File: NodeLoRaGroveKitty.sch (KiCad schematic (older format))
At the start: 39 parts, among them P1 PICKIT PROGRAMMER, P2 Battery, P3 A0, P4 D9, P5 USB-Serial, P6 I2C, SW1 SW_BOOT, SW2 SW_RESET, U1 AP2114, U2 MCP73831T-2ATI/OT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

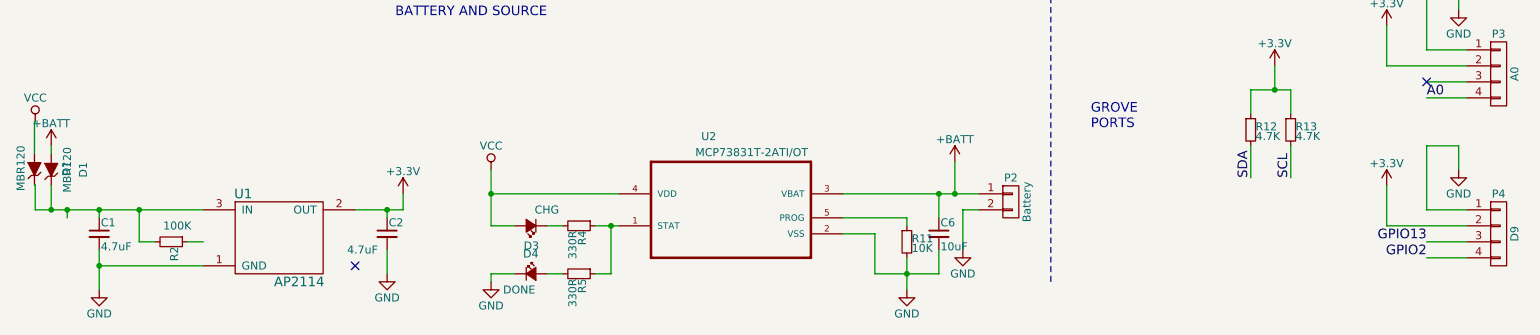
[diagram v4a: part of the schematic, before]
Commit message: Change D2 for D13
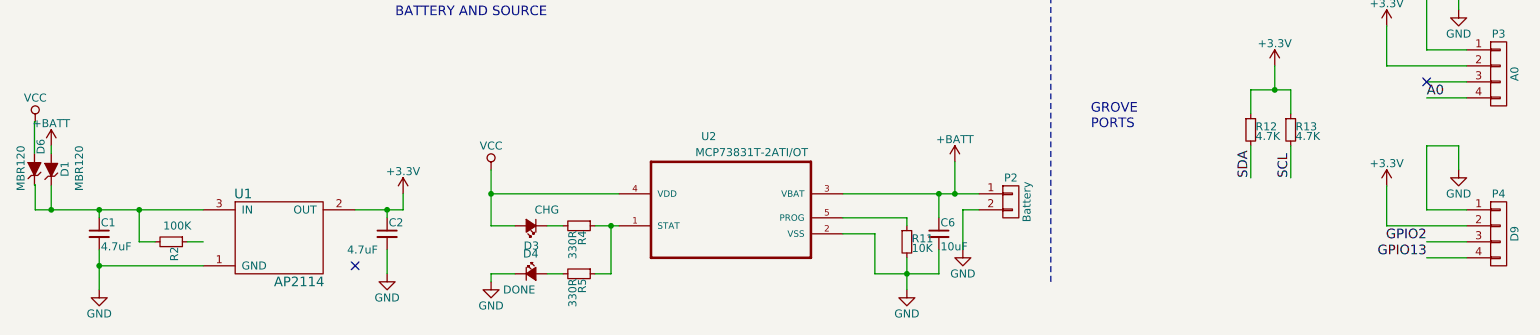
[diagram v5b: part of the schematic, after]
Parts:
- gave numbers to parts that had none: 1
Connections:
- net GPIO13: now also P4.4 (P4); no longer P4.3 (P3)
- net GPIO2: now also P4.3 (P3); no longer P4.4 (P4)
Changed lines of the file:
@@
 NoConn ~ 1450 2250
 $Comp
-L +3.3V #PWR01
+L +3.3V #PWR9
 U 1 1 57D06DBD
 P 3200 800
-F 0 "#PWR01" H 3200 650 50  0001 C CNN
+F 0 "#PWR9" H 3200 650 50  0001 C CNN
 F 1 "+3.3V" H 3200 940 50  0000 C CNN
 F 2 "" H 3200 800 50  0000 C CNN
@@
 $EndComp
 $Comp
-L GND #PWR02
+L GND #PWR10
 U 1 1 57D06E12
 P 3250 3400
-F 0 "#PWR02" H 3250 3150 50  0001 C CNN
+F 0 "#PWR10" H 3250 3150 50  0001 C CNN
 F 1 "GND" H 3250 3250 50  0000 C CNN
 F 2 "" H 3250 3400 50  0000 C CNN
@@
 $EndComp
 $Comp
-L GND #PWR03
+L GND #PWR4
 U 1 1 57D1B92A
 P 1000 6600
-F 0 "#PWR03" H 1000 6350 50  0001 C CNN
+F 0 "#PWR4" H 1000 6350 50  0001 C CNN
 F 1 "GND" H 1000 6450 50  0000 C CNN
 F 2 "" H 1000 6600 50  0000 C CNN
@@
 U 1 1 57D1B9F5
 P 700 5850
-F 0 "D1" H 700 5650 50  0000 C CNN
-F 1 "MBR120" H 700 5750 50  0000 C CNN
+F 0 "D1" H 705 5765 50  0000 C CNN
+F 1 "MBR120" H 710 5675 50  0000 C CNN
 F 2 "Diodes_SMD:SOD-123" H 700 5850 50  0001 C CNN
 F 3 "" H 700 5850 50  0000 C CNN
@@
 NoConn ~ 2600 6450
 $Comp
-L +3.3V #PWR04
+L +3.3V #PWR7
 U 1 1 57D1BDB1
 P 2900 6000
-F 0 "#PWR04" H 2900 5850 50  0001 C CNN
+F 0 "#PWR7" H 2900 5850 50  0001 C CNN
 F 1 "+3.3V" H 2900 6140 50  0000 C CNN
 F 2 "" H 2900 6000 50  0000 C CNN
@@
 $EndComp
 $Comp
-L VCC #PWR05
+L VCC #PWR2
 U 1 1 57D1BE36
 P 600 5550
-F 0 "#PWR05" H 600 5400 50  0001 C CNN
+F 0 "#PWR2" H 600 5400 50  0001 C CNN
 F 1 "VCC" H 600 5700 50  0000 C CNN
 F 2 "" H 600 5550 50  0000 C CNN
@@
 $EndComp
 $Comp
-L +BATT #PWR06
+L +BATT #PWR3
 U 1 1 57D1BE7A
 P 700 5700
-F 0 "#PWR06" H 700 5550 50  0001 C CNN
+F 0 "#PWR3" H 700 5550 50  0001 C CNN
 F 1 "+BATT" H 700 5840 50  0000 C CNN
 F 2 "" H 700 5700 50  0000 C CNN
@@
 $EndComp
 $Comp
-L GND #PWR07
+L GND #PWR23
 U 1 1 57D1D194
 P 6050 6600
-F 0 "#PWR07" H 6050 6350 50  0001 C CNN
+F 0 "#PWR23" H 6050 6350 50  0001 C CNN
 F 1 "GND" H 6050 6450 50  0000 C CNN
 F 2 "" H 6050 6600 50  0000 C CNN
@@
 $EndComp
 $Comp
-L VCC #PWR08
+L VCC #PWR12
 U 1 1 57D1D1DE
 P 3450 5850
-F 0 "#PWR08" H 3450 5700 50  0001 C CNN
+F 0 "#PWR12" H 3450 5700 50  0001 C CNN
 F 1 "VCC" H 3450 6000 50  0000 C CNN
 F 2 "" H 3450 5850 50  0000 C CNN
@@
 $EndComp
 $Comp
-L +BATT #PWR09
+L +BATT #PWR24
 U 1 1 57D1DA2B
 P 6350 5800
-F 0 "#PWR09" H 6350 5650 50  0001 C CNN
+F 0 "#PWR24" H 6350 5650 50  0001 C CNN
 F 1 "+BATT" H 6350 5940 50  0000 C CNN
 F 2 "" H 6350 5800 50  0000 C CNN
@@
 $EndComp
 $Comp
-L GND #PWR010
+L GND #PWR25
 U 1 1 57D1DBC4
 P 6400 6350
-F 0 "#PWR010" H 6400 6100 50  0001 C CNN
+F 0 "#PWR25" H 6400 6100 50  0001 C CNN
 F 1 "GND" H 6400 6200 50  0000 C CNN
 F 2 "" H 6400 6350 50  0000 C CNN
@@
 $EndComp
 $Comp
-L GND #PWR011
+L GND #PWR13
 U 1 1 57D1E0B8
 P 3450 6550
-F 0 "#PWR011" H 3450 6300 50  0001 C CNN
+F 0 "#PWR13" H 3450 6300 50  0001 C CNN
 F 1 "GND" H 3450 6400 50  0000 C CNN
 F 2 "" H 3450 6550 50  0000 C CNN
@@
 $EndComp
 $Comp
-L +3.3V #PWR012
+L +3.3V #PWR28
 U 1 1 57D1F885
 P 8350 5200
-F 0 "#PWR012" H 8350 5050 50  0001 C CNN
+F 0 "#PWR28" H 8350 5050 50  0001 C CNN
 F 1 "+3.3V" H 8350 5340 50  0000 C CNN
 F 2 "" H 8350 5200 50  0000 C CNN
@@
 $EndComp
 $Comp
-L GND #PWR013
+L GND #PWR17
 U 1 1 57D20110
 P 4400 1550
-F 0 "#PWR013" H 4400 1300 50  0001 C CNN
+F 0 "#PWR17" H 4400 1300 50  0001 C CNN
 F 1 "GND" H 4400 1400 50  0000 C CNN
 F 2 "" H 4400 1550 50  0000 C CNN
@@
 $EndComp
 $Comp
-L +3.3V #PWR014
+L +3.3V #PWR22
 U 1 1 57D20695
 P 5300 900
-F 0 "#PWR014" H 5300 750 50  0001 C CNN
+F 0 "#PWR22" H 5300 750 50  0001 C CNN
 F 1 "+3.3V" H 5300 1040 50  0000 C CNN
 F 2 "" H 5300 900 50  0000 C CNN
@@
 SDA
 $Comp
-L GND #PWR015
+L GND #PWR36
 U 1 1 57D20B0E
 P 10700 4850
-F 0 "#PWR015" H 10700 4600 50  0001 C CNN
+F 0 "#PWR36" H 10700 4600 50  0001 C CNN
 F 1 "GND" H 10700 4700 50  0000 C CNN
 F 2 "" H 10700 4850 50  0000 C CNN
@@
 $EndComp
 $Comp
-L +3.3V #PWR016
+L +3.3V #PWR14
 U 1 1 57D218AC
 P 3650 2350
-F 0 "#PWR016" H 3650 2200 50  0001 C CNN
+F 0 "#PWR14" H 3650 2200 50  0001 C CNN
 F 1 "+3.3V" H 3650 2490 50  0000 C CNN
 F 2 "" H 3650 2350 50  0000 C CNN
@@
 A0
 $Comp
-L GND #PWR017
+L GND #PWR31
 U 1 1 57D2307B
 P 9500 4850
-F 0 "#PWR017" H 9500 4600 50  0001 C CNN
+F 0 "#PWR31" H 9500 4600 50  0001 C CNN
 F 1 "GND" H 9500 4700 50  0000 C CNN
 F 2 "" H 9500 4850 50  0000 C CNN
@@
 $EndComp
 Text Label 9300 6400 2    60   ~ 0
+GPIO13
+Text Label 9300 6300 2    60   ~ 0
 GPIO2
-Text Label 9300 6300 2    60   ~ 0
-GPIO13
-$Comp
-L GND #PWR018
+$Comp
+L GND #PWR32
 U 1 1 57D230E6
 P 9500 5850
-F 0 "#PWR018" H 9500 5600 50  0001 C CNN
+F 0 "#PWR32" H 9500 5600 50  0001 C CNN
 F 1 "GND" H 9500 5700 50  0000 C CNN
 F 2 "" H 9500 5850 50  0000 C CNN
@@
 $EndComp
 $Comp
-L GND #PWR019
+L GND #PWR11
 U 1 1 57D23805
 P 3450 1250
-F 0 "#PWR019" H 3450 1000 50  0001 C CNN
+F 0 "#PWR11" H 3450 1000 50  0001 C CNN
 F 1 "GND" H 3450 1100 50  0000 C CNN
 F 2 "" H 3450 1250 50  0000 C CNN
@@
 $EndComp
 $Comp
-L GND #PWR021
+L GND #PWR15
 U 1 1 57D25846
 P 3850 1250
-F 0 "#PWR021" H 3850 1000 50  0001 C CNN
+F 0 "#PWR15" H 3850 1000 50  0001 C CNN
 F 1 "GND" H 3850 1100 50  0000 C CNN
 F 2 "" H 3850 1250 50  0000 C CNN
@@
 $EndComp
 $Comp
-L GND #PWR022
+L GND #PWR5
 U 1 1 57D2E394
 P 1500 850
-F 0 "#PWR022" H 1500 600 50  0001 C CNN
+F 0 "#PWR5" H 1500 600 50  0001 C CNN
 F 1 "GND" H 1500 700 50  0000 C CNN
 F 2 "" H 1500 850 50  0000 C CNN
@@
 $EndComp
 $Comp
-L GND #PWR023
+L GND #PWR1
 U 1 1 57D2E541
 P 600 950
-F 0 "#PWR023" H 600 700 50  0001 C CNN
+F 0 "#PWR1" H 600 700 50  0001 C CNN
 F 1 "GND" H 600 800 50  0000 C CNN
 F 2 "" H 600 950 50  0000 C CNN
@@
 $EndComp
 $Comp
-L GND #PWR024
+L GND #PWR6
 U 1 1 57D3198A
 P 2800 6500
-F 0 "#PWR024" H 2800 6250 50  0001 C CNN
+F 0 "#PWR6" H 2800 6250 50  0001 C CNN
 F 1 "GND" H 2800 6350 50  0000 C CNN
 F 2 "" H 2800 6500 50  0000 C CNN
@@
 $EndComp
 $Comp
-L GND #PWR025
+L GND #PWR8
 U 1 1 57D378F3
 P 3150 3000
-F 0 "#PWR025" H 3150 2750 50  0001 C CNN
+F 0 "#PWR8" H 3150 2750 50  0001 C CNN
 F 1 "GND" H 3150 2850 50  0000 C CNN
 F 2 "" H 3150 3000 50  0000 C CNN
@@
 RST
 $Comp
-L GND #PWR026
+L GND #PWR34
 U 1 1 5807D443
 P 9925 1885
-F 0 "#PWR026" H 9925 1635 50  0001 C CNN
+F 0 "#PWR34" H 9925 1635 50  0001 C CNN
 F 1 "GND" H 9925 1735 50  0000 C CNN
 F 2 "" H 9925 1885 50  0000 C CNN
@@
 $EndComp
 $Comp
-L +3.3V #PWR027
+L +3.3V #PWR27
 U 1 1 5807DA5B
 P 7425 1885
-F 0 "#PWR027" H 7425 1735 50  0001 C CNN
+F 0 "#PWR27" H 7425 1735 50  0001 C CNN
 F 1 "+3.3V" H 7425 2025 50  0000 C CNN
 F 2 "" H 7425 1885 50  0000 C CNN
@@
 $EndComp
 $Comp
-L GND #PWR028
+L GND #PWR20
 U 1 1 58092ECC
 P 4840 3295
-F 0 "#PWR028" H 4840 3045 50  0001 C CNN
+F 0 "#PWR20" H 4840 3045 50  0001 C CNN
 F 1 "GND" H 4840 3145 50  0000 C CNN
 F 2 "" H 4840 3295 50  0000 C CNN
@@
 $EndComp
 $Comp
-L +3.3V #PWR029
+L +3.3V #PWR18
 U 1 1 58094181
 P 4540 2635
-F 0 "#PWR029" H 4540 2485 50  0001 C CNN
+F 0 "#PWR18" H 4540 2485 50  0001 C CNN
 F 1 "+3.3V" H 4540 2775 50  0000 C CNN
 F 2 "" H 4540 2635 50  0000 C CNN
@@
 $EndComp
 $Comp
-L GND #PWR030
+L GND #PWR19
 U 1 1 58098088
 P 4560 3870
-F 0 "#PWR030" H 4560 3620 50  0001 C CNN
+F 0 "#PWR19" H 4560 3620 50  0001 C CNN
 F 1 "GND" H 4560 3720 50  0000 C CNN
 F 2 "" H 4560 3870 50  0000 C CNN
@@
 TX
 $Comp
-L GND #PWR031
+L GND #PWR33
 U 1 1 5809B44C
 P 9805 3850
-F 0 "#PWR031" H 9805 3600 50  0001 C CNN
+F 0 "#PWR33" H 9805 3600 50  0001 C CNN
 F 1 "GND" H 9805 3700 50  0000 C CNN
 F 2 "" H 9805 3850 50  0000 C CNN
@@
 $EndComp
 $Comp
-L VCC #PWR032
+L VCC #PWR37
 U 1 1 5809B516
 P 10840 3935
-F 0 "#PWR032" H 10840 3785 50  0001 C CNN
+F 0 "#PWR37" H 10840 3785 50  0001 C CNN
 F 1 "VCC" H 10840 4085 50  0000 C CNN
 F 2 "" H 10840 3935 50  0000 C CNN
@@
 $EndComp
 $Comp
-L PWR_FLAG #FLG033
+L PWR_FLAG #FLG1
 U 1 1 5809BB20
 P 10550 3955
-F 0 "#FLG033" H 10550 4050 50  0001 C CNN
+F 0 "#FLG1" H 10550 4050 50  0001 C CNN
 F 1 "PWR_FLAG" H 10550 4135 50  0000 C CNN
 F 2 "" H 10550 3955 50  0000 C CNN
@@
 $EndComp
 $Comp
-L GND #PWR034
+L GND #PWR16
 U 1 1 5809F5BD
 P 4380 2115
-F 0 "#PWR034" H 4380 1865 50  0001 C CNN
+F 0 "#PWR16" H 4380 1865 50  0001 C CNN
 F 1 "GND" H 4380 1965 50  0000 C CNN
 F 2 "" H 4380 2115 50  0000 C CNN
@@
 $EndComp
 $Comp
-L +3.3V #PWR035
+L +3.3V #PWR29
 U 1 1 58514B84
 P 9050 4950
-F 0 "#PWR035" H 9050 4800 50  0001 C CNN
+F 0 "#PWR29" H 9050 4800 50  0001 C CNN
 F 1 "+3.3V" H 9050 5090 50  0000 C CNN
 F 2 "" H 9050 4950 50  0000 C CNN
@@
 $EndComp
 $Comp
-L +3.3V #PWR036
+L +3.3V #PWR35
 U 1 1 58514F58
 P 10250 4950
-F 0 "#PWR036" H 10250 4800 50  0001 C CNN
+F 0 "#PWR35" H 10250 4800 50  0001 C CNN
 F 1 "+3.3V" H 10250 5090 50  0000 C CNN
 F 2 "" H 10250 4950 50  0000 C CNN
@@
 $EndComp
 $Comp
-L +3.3V #PWR037
+L +3.3V #PWR30
 U 1 1 585150D6
 P 9050 5950
-F 0 "#PWR037" H 9050 5800 50  0001 C CNN
+F 0 "#PWR30" H 9050 5800 50  0001 C CNN
 F 1 "+3.3V" H 9050 6090 50  0000 C CNN
 F 2 "" H 9050 5950 50  0000 C CNN
@@
 GPIO2
 $Comp
-L +3.3V #PWR038
+L +3.3V #PWR21
 U 1 1 5854483F
 P 5160 2620
-F 0 "#PWR038" H 5160 2470 50  0001 C CNN
+F 0 "#PWR21" H 5160 2470 50  0001 C CNN
 F 1 "+3.3V" H 5160 2760 50  0000 C CNN
 F 2 "" H 5160 2620 50  0000 C CNN
@@
 $EndComp
 $Comp
-L ZENERsmall D?
+L ZENERsmall D6
 U 1 1 58924335
 P 595 5845
-F 0 "D?" H 595 5645 50  0000 C CNN
+F 0 "D6" H 735 5805 50  0000 C CNN
 F 1 "MBR120" H 600 5930 50  0000 C CNN
 F 2 "Diodes_SMD:SOD-123" H 595 5845 50  0001 C CNN
@@
 Wire Wire Line
 	1000 6100 1000 6150
-Connection ~ 800  6100
-Wire Wire Line
-	800  6100 800  6150
 Connection ~ 1250 6100
 Wire Wire Line
@@
 NoConn ~ 1450 2050
 $Comp
-L +3.3V #PWR?
+L +3.3V #PWR26
 U 1 1 58926B64
 P 6840 3940
-F 0 "#PWR?" H 6840 3790 50  0001 C CNN
+F 0 "#PWR26" H 6840 3790 50  0001 C CNN
 F 1 "+3.3V" H 6840 4080 50  0000 C CNN
 F 2 "" H 6840 3940 50  0000 C CNN

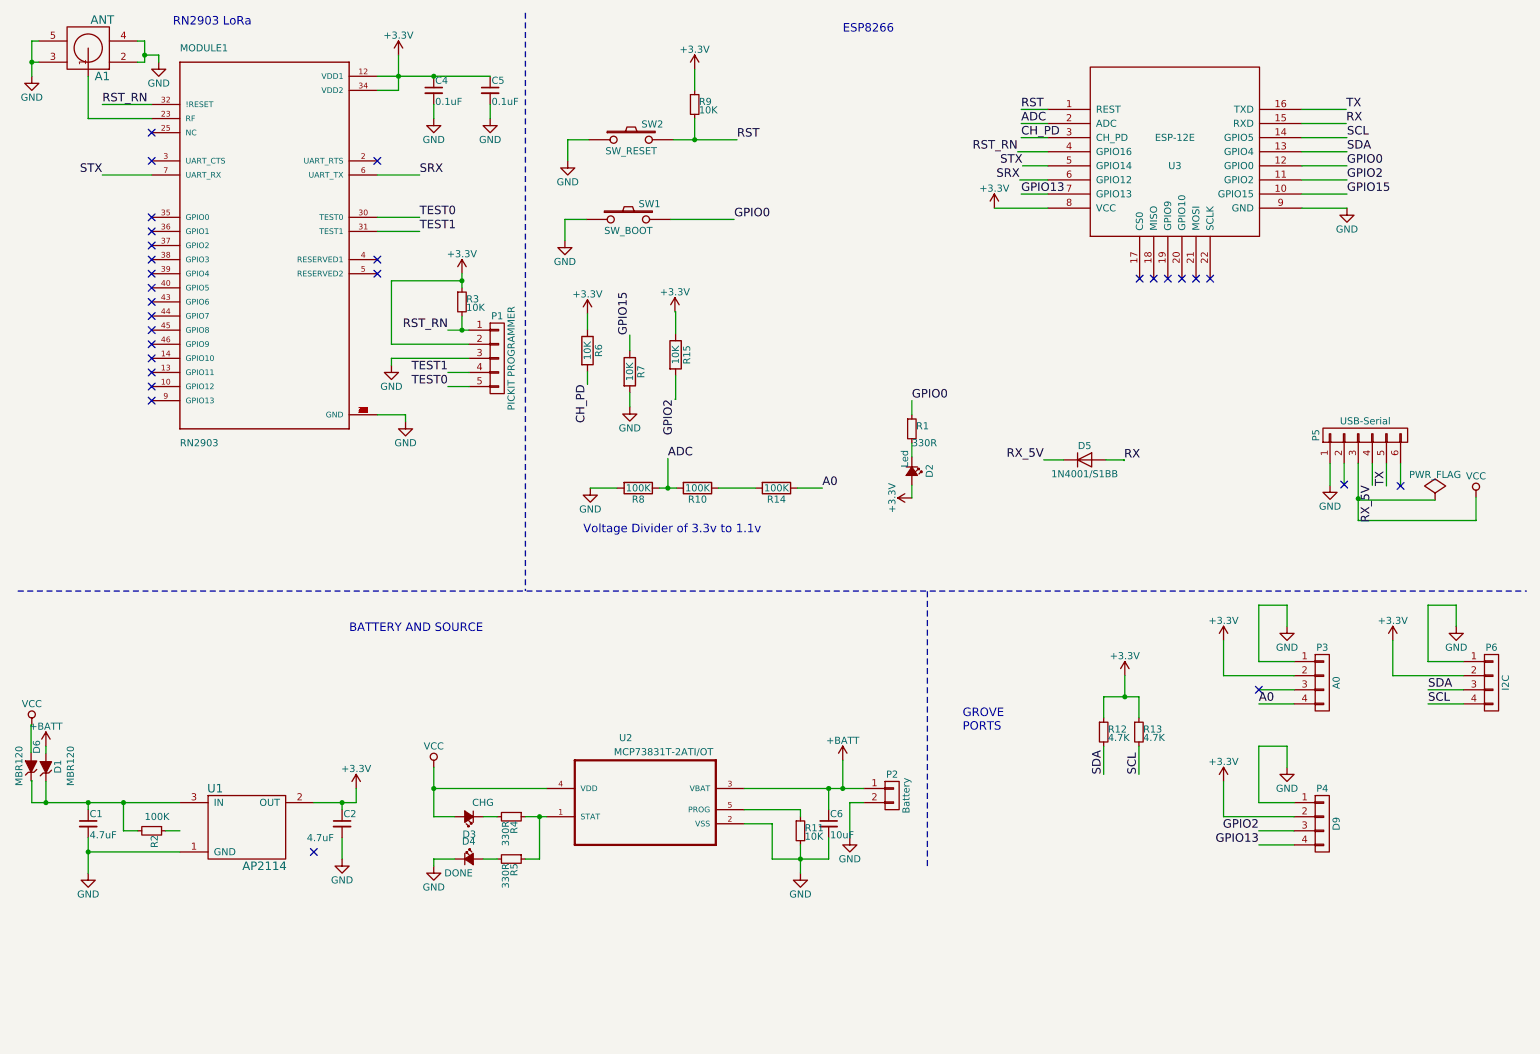
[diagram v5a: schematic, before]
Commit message: Added autoreset and USB_Serial
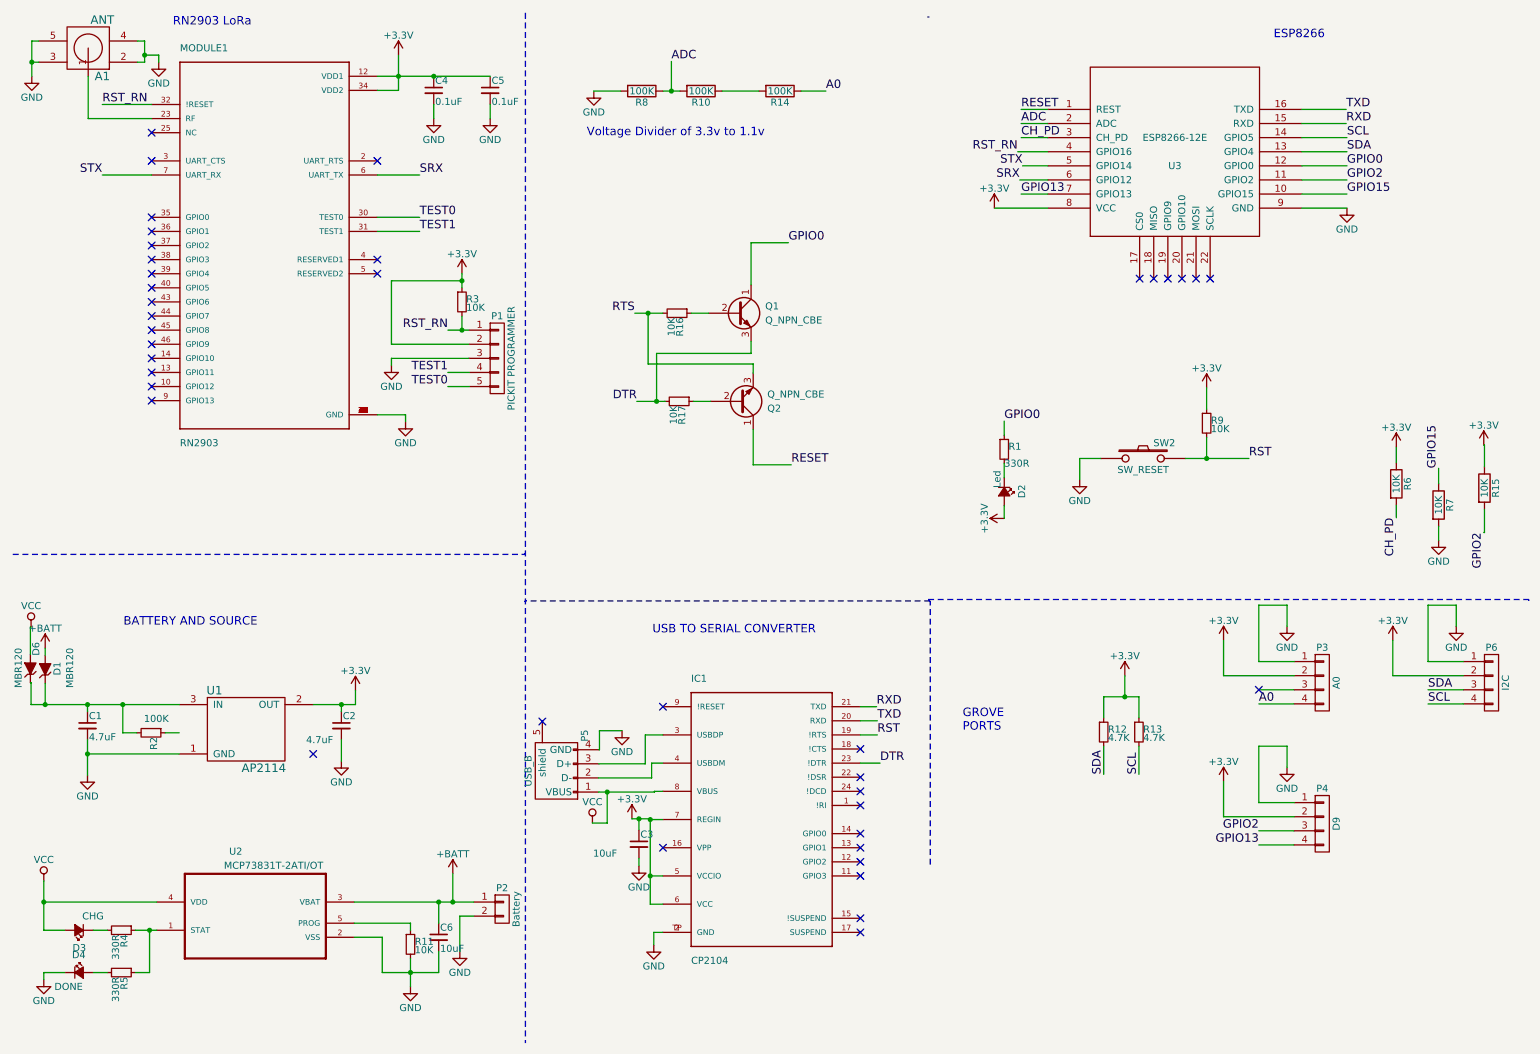
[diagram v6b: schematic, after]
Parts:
- removed D5: 1N4001/S1BB, Diodes_SMD:SMB_Handsoldering, symbol D
- removed P5: USB-Serial, Socket_Strips:Socket_Strip_Straight_1x06, symbol CONN_01X06
- removed SW1: SW_BOOT, TIH:SW_B3U-1000P, symbol SW_PUSH
- added C3: 10uF, symbol C_Small
- added IC1: CP2104, QFN24-PAD, symbol CP2104
- added P5: USB_B, symbol USB_B
- added Q1, Q2: Q_NPN_CBE, symbol Q_NPN_CBE
- added R16, R17: 10K, symbol R_Small
- P3, P4, P6: manf# S4B-PH-K-S(LF)(SN) -> 110990037
- U3: value ESP-12E -> ESP8266-12E; manf# (none) -> ESP8266-12E
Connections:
- net +3V3: now also C3.1, IC1.5 (VCCIO), IC1.6 (VCC), IC1.7 (REGIN)
- net GND: now also C3.2, IC1.2 (GND), IC1.TP (GND), P5.4 (GND)
- net GPIO0: now also Q1.1 (C)
- net RST: now also IC1.19 (!RTS); no longer U3.1 (REST)
- net VCC: now also IC1.8 (VBUS), P5.1 (VBUS)
- net RX renamed RXD
- net RXD: now also IC1.21 (TXD)
- net TX renamed TXD
- net TXD: now also IC1.20 (RXD)
- new net: IC1.3 (USBDP), P5.3 (D+)
- new net: IC1.4 (USBDM), P5.2 (D-)
- new net: Q2.2 (B), R17.1
- new net: Q1.2 (B), R16.1
- new net DTR: IC1.23 (!DTR), Q1.3 (E), R17.2
- new net RESET: Q2.1 (C), U3.1 (REST)
- new net RTS: Q2.3 (E), R16.2
- no-connect marks 29 -> 40
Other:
- note added: "USB TO SERIAL CONVERTER"
- moved on the sheet: C1, C2, C6, D1, D2, D3, D4, D6, P2, R1, R10, R11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
